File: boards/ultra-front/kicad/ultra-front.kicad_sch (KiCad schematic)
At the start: 36 parts, among them J1 FPC-05F-20PH20, J2 FPC-05FB-12PH20, Q1 AO3400A, SW1 TS-1187A-B-A-B, SW2 TS-1187A-B-A-B, SW3 TS-1187A-B-A-B, SW4 EC11E1834403, U1 TCA9535PWR, U2 IRM-H638T/TR2

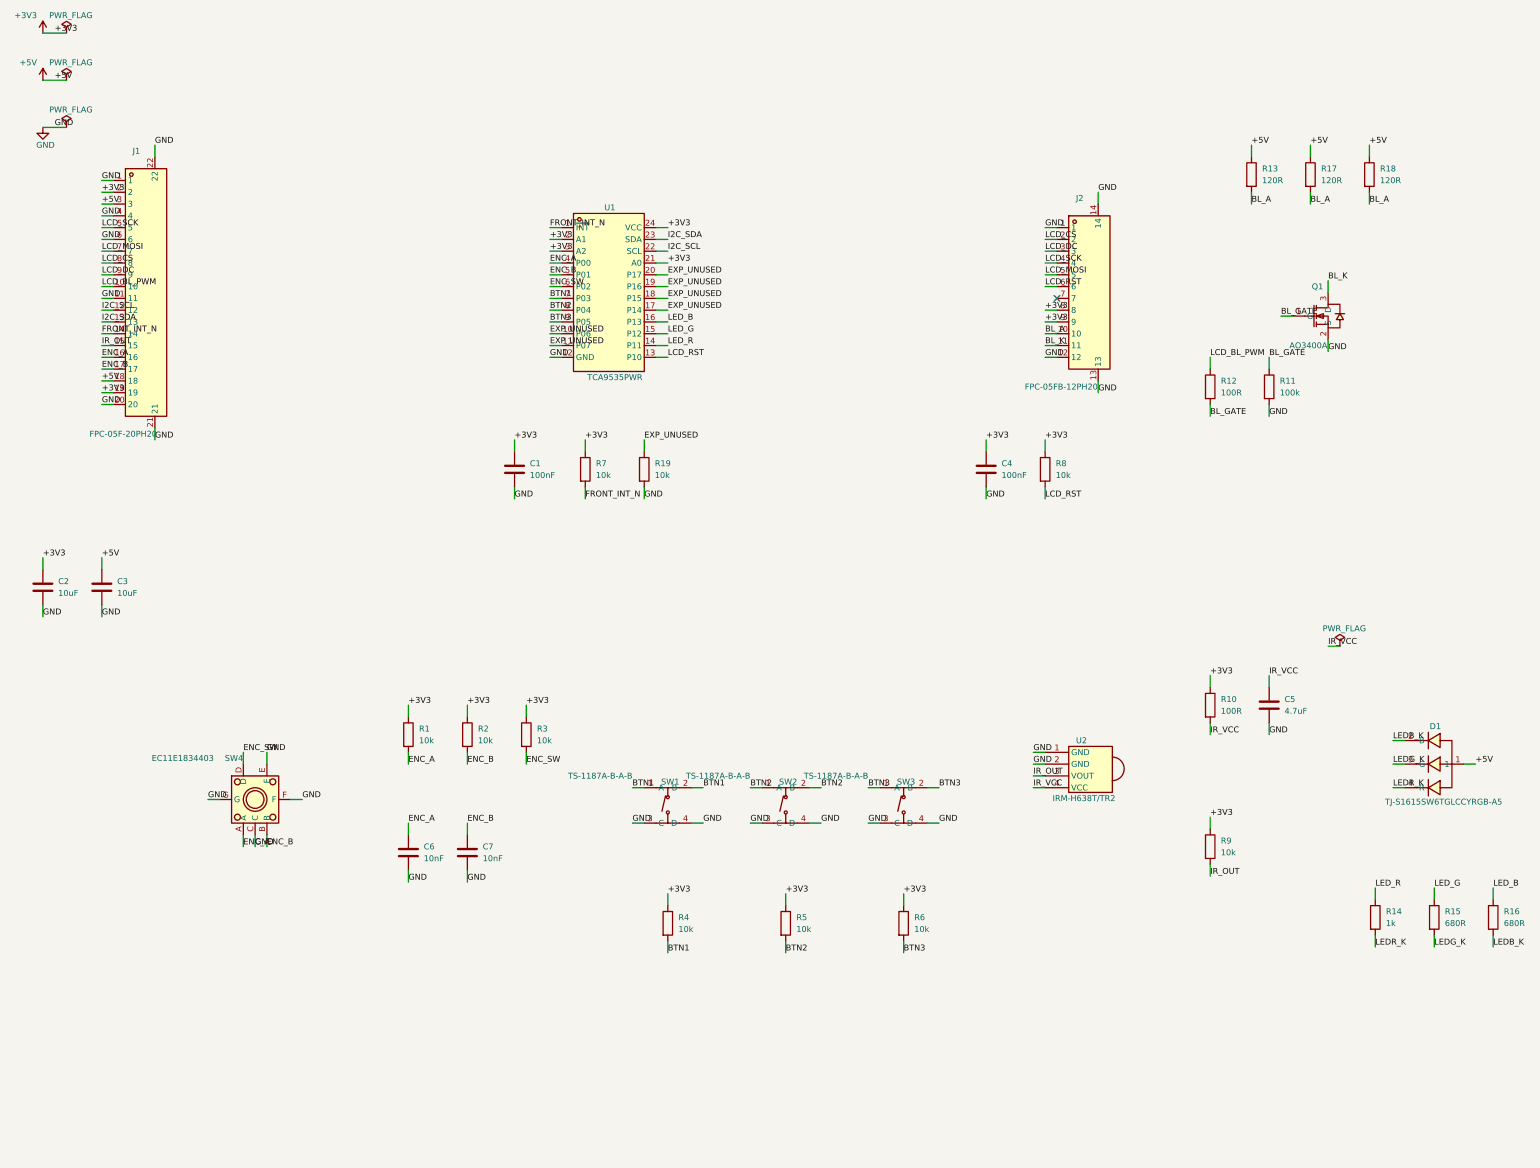
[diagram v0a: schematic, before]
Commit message: ultra-front: ESD clamps at the switches (R5-UF-2)
D2/D3 PESD5V0S2BT (C49338, as on core): D2 on BTN2/BTN1 between SW1 and
SW2, D3 on BTN3/ENC_SW between SW2 and SW3, each GND pin on its own via.
Schematic generator, parts, PCB (board_update + kicad/gen/esd_eco.py), fab
regenerated, README, bom-estimate and product.md totals updated.
docs/boards/ultra-front-esd.md has the layout reasoning.

Co-Authored-By: Claude Opus 5.5 <noreply@anthropic.com>
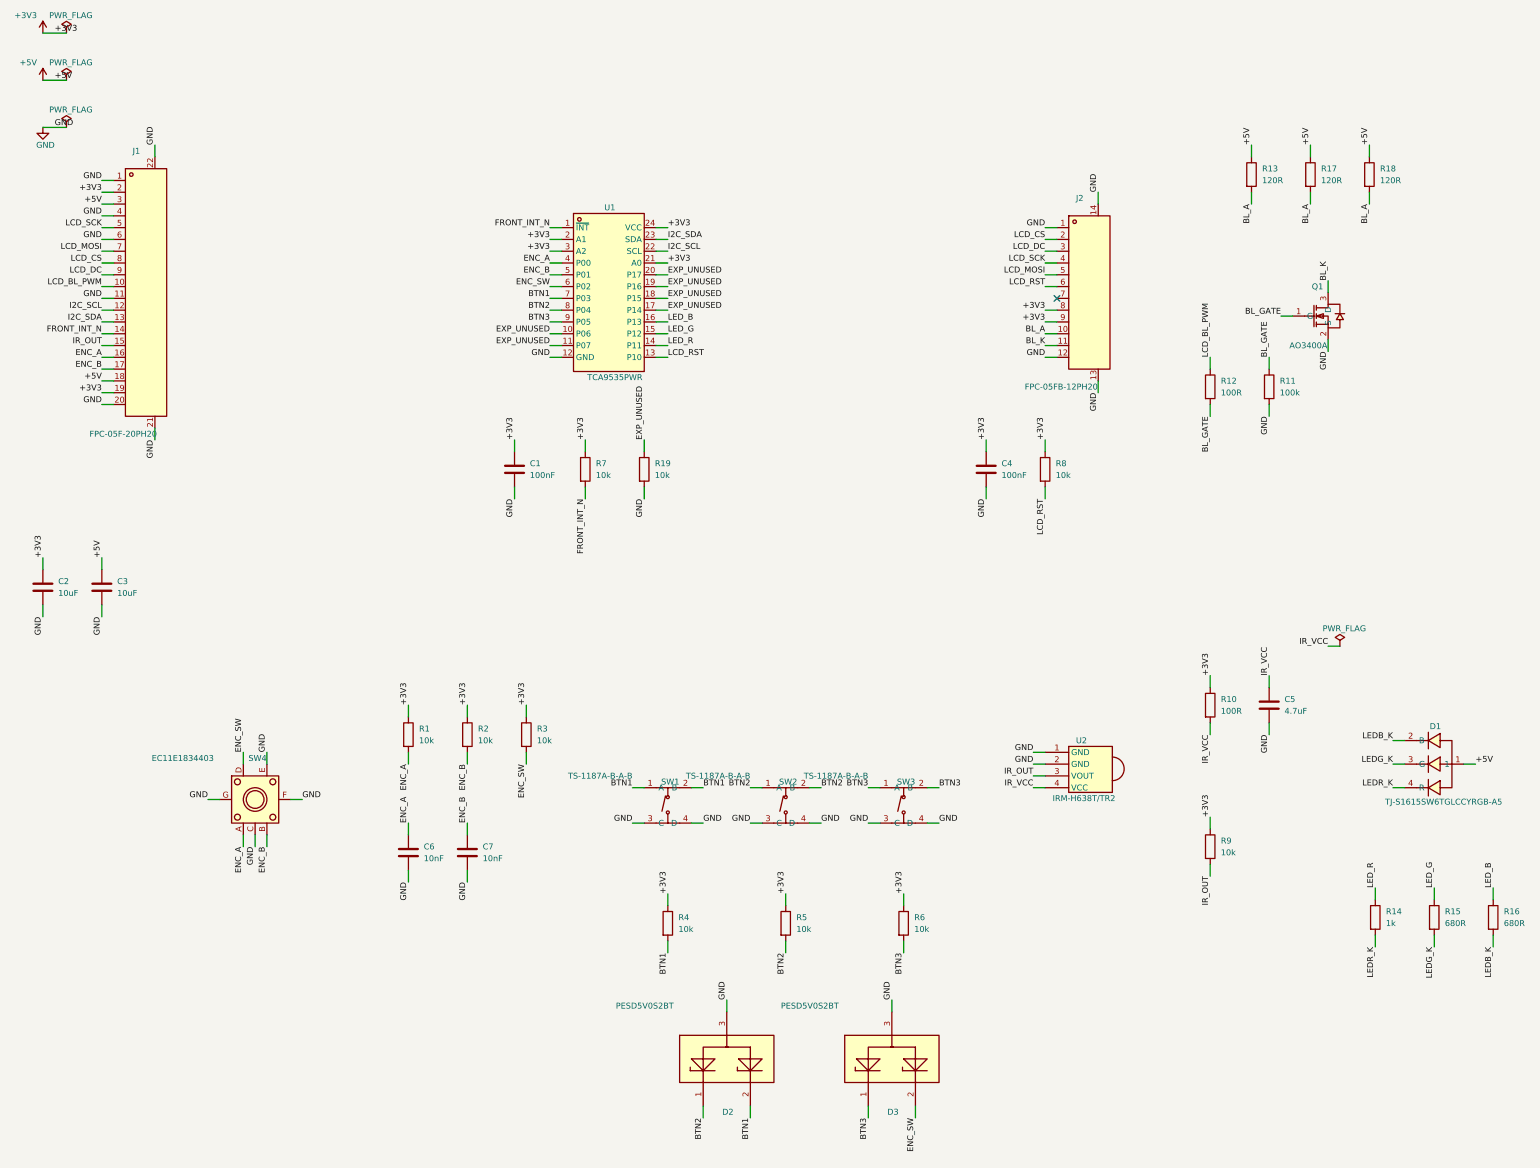
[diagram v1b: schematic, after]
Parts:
- added D2, D3: PESD5V0S2BT, aiee:SOT-23_L2.9-W1.3-P1.90-LS2.4-BR, symbol aiee:PESD5V0S2BT,215
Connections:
- net BTN1: now also D2.2
- net BTN2: now also D2.1
- net BTN3: now also D3.1
- net ENC_SW: now also D3.2
- net GND: now also D2.3, D3.3
